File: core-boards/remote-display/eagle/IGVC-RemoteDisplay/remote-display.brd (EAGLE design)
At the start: 54.5 x 43 mm, 20 parts, among them IC1 ATMEGA2560-15AU, J1 ULCD-144G2, SW1 SPST_TACT-EVQQ2, U1 CC1101-MODULE, X1 16MHz, X2 MSTBA2

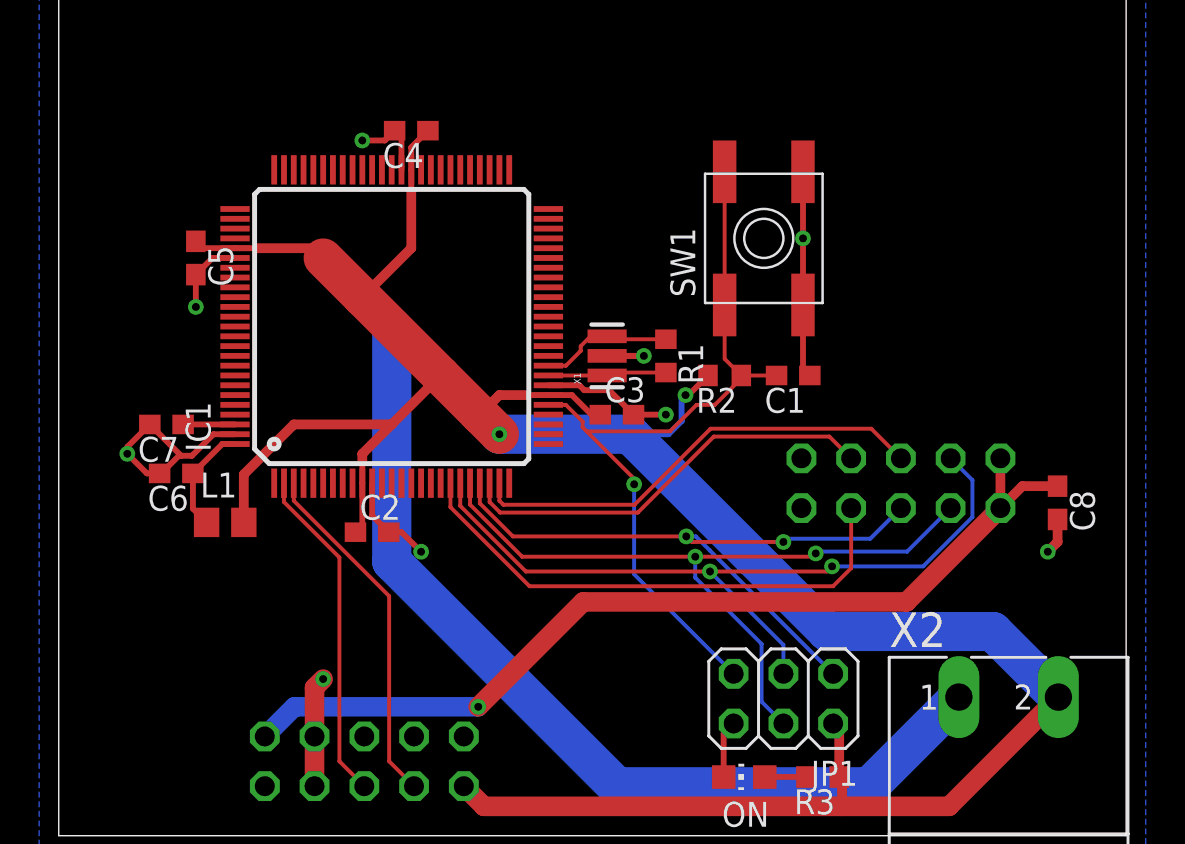
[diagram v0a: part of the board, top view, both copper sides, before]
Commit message: Replaced the MEGA2560 with a MEGA328p
This is just an option; if there are reasons for using the 2560, this can certainly be reverted
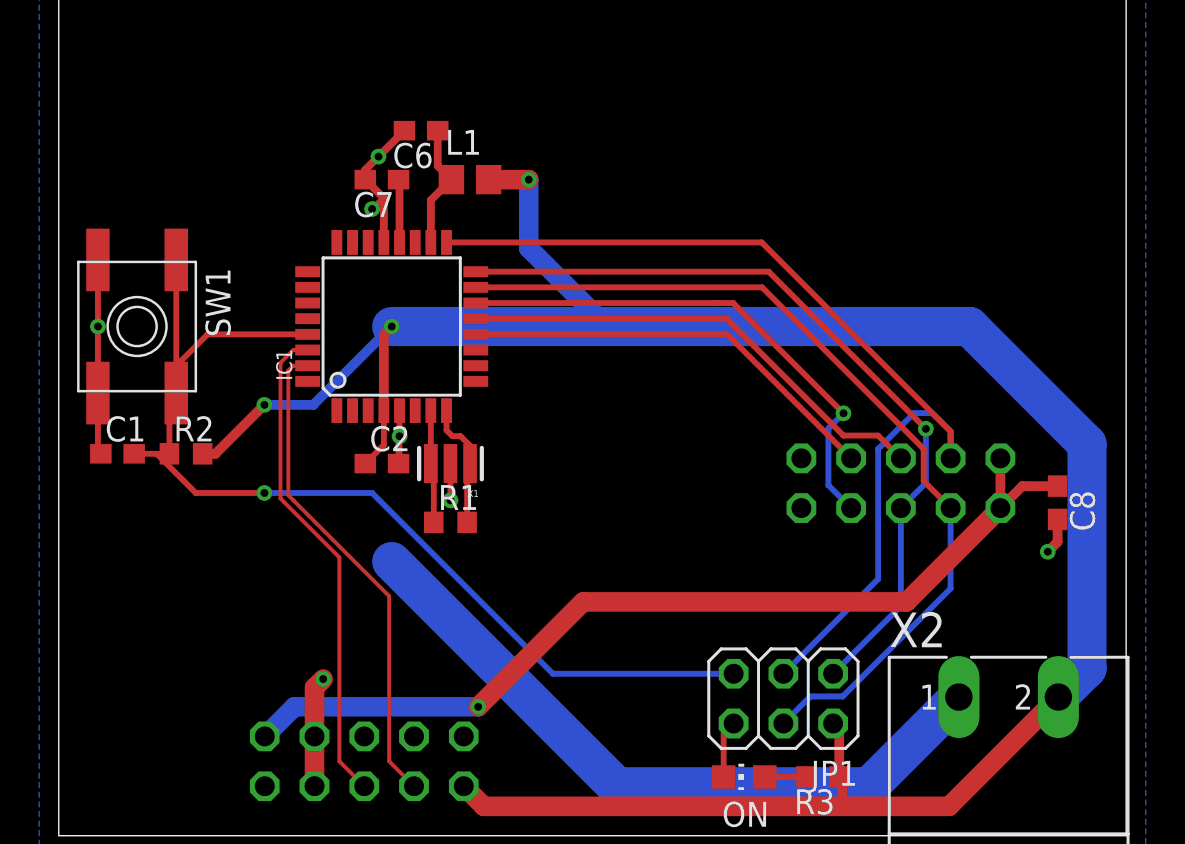
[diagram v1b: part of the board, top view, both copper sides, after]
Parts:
- removed C3, C4, C5: 100nF, resistor:C0603
- IC1: value ATMEGA2560-15AU -> ATMEGA8; device IGVC-Remote:TQFP100 -> atmel:TQFP32-08
- moved C1 34.7 mm to (3.00, 19.5), turned to 0 degrees
- moved SW1 32.3 mm to (4.00, 26.0), turned to 270 degrees
- moved R2 27.8 mm to (6.50, 19.5), turned to 0 degrees
- moved C6 21.5 mm to (18.5, 36.0)
- moved L1 21.5 mm to (21.0, 33.5)
- moved C7 16.7 mm to (16.5, 33.5)
- moved R1 13.9 mm to (20.0, 16.0), turned to 0 degrees
- moved X1 9.71 mm to (20.0, 19.0), turned to 180 degrees
- moved C2 3.54 mm to (16.5, 19.0)
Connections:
- net +5V: now also IC1.4; no longer C3.1, C4.1, C5.1, IC1.10, IC1.31, IC1.61, IC1.80
- net AREF: now also IC1.20; no longer IC1.98
- net AVCC: now also IC1.18; no longer IC1.100
- net CS: now also IC1.14; no longer IC1.19
- net GDO0: now also IC1.12; no longer IC1.23
- net GDO2: now also IC1.13; no longer IC1.24
- net GND: now also IC1.21, IC1.5; no longer C3.2, C4.2, C5.2, IC1.11, IC1.32, IC1.62, IC1.81, IC1.99
- net MISO: now also IC1.16; no longer IC1.22
- net MOSI: now also IC1.15; no longer IC1.21
- net RESET: now also IC1.29; no longer IC1.30
- net RX: now also IC1.30; no longer IC1.2
- net SCK: now also IC1.17; no longer IC1.20
- net TX: now also IC1.31; no longer IC1.3
- net XTAL1: now also IC1.7; no longer IC1.34
- net XTAL2: now also IC1.8; no longer IC1.33
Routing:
- net GND: track 102.5 -> 69.8 mm, vias 9 -> 7
- net +5V: track 134.8 -> 120.1 mm, vias 2 -> 3
- net RESET: track 39.9 -> 53.3 mm
- net SCK: track 40.1 -> 50.8 mm, vias 2 -> 0
- net RX: track 17.2 -> 25.0 mm
- net MOSI: track 38.1 -> 45.4 mm, vias 2 -> 0
- net TX: track 18.0 -> 25.0 mm
- net MISO: track 34.5 -> 40.8 mm, vias 2 -> 1
- net XTAL1: track 6.82 -> 5.77 mm
- net GDO2: track 23.7 -> 24.7 mm
- net AVCC: track 5.56 -> 6.43 mm
- net AREF: track 2.65 -> 3.23 mm
- net CS: track 26.8 -> 26.7 mm, vias 0 -> 1

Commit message: 20191117 Reworked schematic
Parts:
- removed J1: ULCD-144G2, IGVC-Remote:ULCD-144G2
- removed X2: MSTBA2, con-phoenix-508:MSTBA2
- added C10, C11: 10uF, rcl:C0603
- added C3: 0.1uF, resistor:C0603
- added C4: 100uF, rcl:PANASONIC_D
- added C5, C9: 1uF, rcl:C0603
- added J4: B2PS-VH(LF)(SN), RoboJackets-Connectors:B2PS-CENTERED
- added R4: 47R, resistor:R0805
- added T1: R-78E5.0-1.0, MotorBoardDev:R-78E
- added U2: ST7920, IGVC-Remote:ST7920-LCD
- added X3: (no value), IGVC-Connector:NRF24L01+PA+LNA
- C1: value 22p -> 22pF
- C2, C6, C7: value 100nF -> 0.1uF
- C8: value 100n -> 0.1uF
- U1: value CC1101-MODULE -> MIC550X; device IGVC-Remote:2X05 -> IGVC-Regulator:SOT23-DBV
- moved U1 140.8 mm to (1.50, -116.5), flipped to the top
- moved C8 68.1 mm to (113.5, 44.0)
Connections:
- removed net CS: IC1.14, U1.7
- removed net LCD_RST: J1.9
- new net LCD_CS: U2.4
- new net N$3: R4.1, U2.19
- new net RF_CS: IC1.14, X3.CSN
- new net VCC: C10.1, C4.+, J4.2, T1.1
- net +3V3: now also C5.1, U1.5, X3.VCC; no longer J1.10, U1.1, U1.2
- net +5V: now also C11.1, C3.1, C9.1, R4.2, T1.3, U1.1, U2.17, U2.2; no longer J1.1, X2.2
- net GDO0: now also X3.CE; no longer U1.8
- net GDO2: now also X3.IRQ; no longer U1.6
- net GND: now also C10.2, C11.2, C3.2, C4.-, C5.2, C9.2, J4.1, T1.2, U1.2, U2.1, U2.15, U2.20, X3.GND; no longer J1.7, J1.8, U1.10, U1.9, X2.1
- net MISO: now also X3.MISO; no longer U1.5
- net MOSI: now also U2.5, X3.MOSI; no longer U1.3
- net RX: no longer J1.5
- net SCK: now also U2.6, X3.SCK; no longer U1.4
- net TX: no longer J1.3
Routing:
- net +5V: track 120.1 -> 0.00 mm, vias 3 -> 0
- net GND: track 69.8 -> 0.00 mm, vias 7 -> 0
- net RESET: track 53.3 -> 0.00 mm, vias 1 -> 0
- net SCK: track 50.8 -> 0.00 mm
- net +3V3: track 48.3 -> 0.00 mm, vias 1 -> 0
- net MOSI: track 45.4 -> 0.00 mm
- net MISO: track 40.8 -> 0.00 mm, vias 1 -> 0
- net CS: track 26.7 -> 0.00 mm, vias 1 -> 0
- net RX: track 25.0 -> 0.00 mm
- net TX: track 25.0 -> 0.00 mm
- net GDO2: track 24.7 -> 0.00 mm
- net GDO0: track 21.8 -> 0.00 mm
- net XTAL2: track 6.51 -> 0.00 mm
- net AVCC: track 6.43 -> 0.00 mm
- net XTAL1: track 5.77 -> 0.00 mm
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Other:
- board size 54.5 x 43 mm -> 117.5 x 70 mm

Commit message: Finished routing, design review pending
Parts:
- removed J4: B2PS-VH(LF)(SN), RoboJackets-Connectors:B2PS-CENTERED
- removed X3: (no value), IGVC-Connector:NRF24L01+PA+LNA
- added D1, D2: RED, led:CHIP-LED0805
- added J1: B2PS-VH(LF)(SN), RoboJackets-Connectors:B2PS-CENTERED
- added R5, R6: 470R, resistor:R0603
- added R7: 10K, resistor:R0603
- added U$1: ROBOBUZZ1.0X, RoboJackets-Aesthetics:ROBOBUZZ_1.0X
- added X2: (no value), IGVC-Connector:NRF24L01+PA+LNA
- C1: value 22pF -> 0.1uF
- C10: value 10uF -> 1uF
- C11: value 10uF -> 22pF; device rcl:C0603 -> resistor:C0603
- C4: value 100uF -> 0.1uF; device rcl:PANASONIC_D -> resistor:C0603
- C5: value 1uF -> 0.1uF; device rcl:C0603 -> resistor:C0603
- C6: value 0.1uF -> 100uF; device resistor:C0603 -> rcl:PANASONIC_D
- C7: value 0.1uF -> 10uF; device resistor:C0603 -> rcl:C0603
- C8: value 0.1uF -> 1uF; device resistor:C0603 -> rcl:C0603
- C9: value 1uF -> 10uF
- R1: value 1M -> 10K; device resistor:R0603 -> adafruit:TRIM-3386
- R2: value 10K -> 47R; device resistor:R0603 -> resistor:R0805
- R3: value 470R -> 1M
- R4: value 47R -> 470R; device resistor:R0805 -> resistor:R0603
- U1: value MIC550X -> ST7920; device IGVC-Regulator:SOT23-DBV -> IGVC-Remote:ST7920-LCD
- U2: value ST7920 -> MIC550X; device IGVC-Remote:ST7920-LCD -> IGVC-Regulator:SOT23-DBV
- moved C11 182.0 mm to (54.0, 28.0), turned to 90 degrees
- moved C10 178.6 mm to (20.0, 35.0), turned to 90 degrees
- moved C4 170.4 mm to (34.5, 15.5)
- moved T1 165.1 mm to (24.5, 26.5), turned to 90 degrees
- moved C9 157.5 mm to (28.5, 28.5), turned to 270 degrees
- moved U1 147.5 mm to (92.0, 0.00), flipped to the bottom
- moved C3 142.1 mm to (36.5, 32.5), turned to 180 degrees
- moved C5 133.3 mm to (15.5, 9.50), turned to 270 degrees
- moved R4 87.1 mm to (15.0, 4.00), turned to 270 degrees
- moved C8 87.0 mm to (27.0, 35.0), turned to 90 degrees
- moved C1 72.8 mm to (74.0, 3.50), turned to 270 degrees
- moved R1 46.0 mm to (66.0, 14.5)
- moved SW1 43.5 mm to (47.5, 28.0), turned to 0 degrees
- moved U2 35.6 mm to (23.5, 35.0), turned to 90 degrees
- moved R3 33.0 mm to (33.0, 35.5)
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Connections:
- removed net RESET: C1.2, IC1.29, JP1.5, R2.1, SW1.B, SW1.B'
- removed net RX: IC1.30
- removed net TX: IC1.31
- removed net VCC: C10.1, C4.+, J4.2, T1.1
- new net !RESET: C11.2, IC1.29, JP1.5, R7.1, SW1.B, SW1.B'
- new net CONTRAST: R1.2, U1.3
- new net STAT1: IC1.24, R5.1
- new net STAT1_LED: D1.A, R5.2
- new net STAT2: IC1.25, R6.1
- new net STAT2_LED: D2.A, R6.2
- new net VIN: C6.+, C7.1, J1.2, T1.1
- net +3V3: now also C10.1, U2.5, X2.VCC; no longer C8.1, U1.5, X3.VCC
- net +5V: now also C1.1, C8.1, R1.3, R4.1, R7.2, U1.17, U1.2, U2.1, U2.3; no longer C11.1, C2.1, R3.1, R4.2, U1.1, U2.17, U2.2
- net AREF: now also C2.1; no longer C7.1
- net AVCC: now also C4.1; no longer C6.1
- net GDO0: now also X2.CE; no longer X3.CE
- net GDO2: now also X2.IRQ; no longer X3.IRQ
- net GND: now also C1.2, C11.1, C4.2, C6.-, D1.C, D2.C, J1.1, R1.1, U1.1, U1.15, U1.20, U2.2, X2.GND; no longer C1.1, C11.2, C4.-, C6.2, J4.1, U1.2, U2.1, U2.15, U2.20, X3.GND
- net LCD_CS: now also IC1.28, U1.4; no longer U2.4
- net MISO: now also X2.MISO; no longer X3.MISO
- net MOSI: now also U1.5, X2.MOSI; no longer U2.5, X3.MOSI
- net N$3: now also R2.1, U1.19; no longer R4.1, U2.19
- net PWR_LED: now also R4.2; no longer R3.2
- net RF_CS: now also X2.CSN; no longer X3.CSN
- net SCK: now also U1.6, X2.SCK; no longer U2.6, X3.SCK
- net XTAL1: now also R3.1; no longer R1.1
- net XTAL2: now also R3.2; no longer R1.2
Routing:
- net +5V: track 0.00 -> 150.9 mm, vias 0 -> 3
- net GND: track 0.00 -> 124.7 mm, vias 0 -> 8
- net MOSI: track 0.00 -> 95.8 mm, vias 0 -> 2
- net SCK: track 0.00 -> 92.8 mm, vias 0 -> 3
- net MISO: track 0.00 -> 59.6 mm, vias 0 -> 1
- net VIN: track 0.00 -> 42.9 mm
- net GDO0: track 0.00 -> 40.7 mm, vias 0 -> 1
- net GDO2: track 0.00 -> 39.2 mm
- net STAT2: track 0.00 -> 38.1 mm, vias 0 -> 2
- net STAT1: track 0.00 -> 37.9 mm, vias 0 -> 2
- net RF_CS: track 0.00 -> 34.0 mm, vias 0 -> 1
- net +3V3: track 0.00 -> 33.9 mm, vias 0 -> 2
- net LCD_CS: track 0.00 -> 32.6 mm
- net !RESET: track 0.00 -> 30.1 mm
- net CONTRAST: track 0.00 -> 9.17 mm
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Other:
- board size 117.5 x 70 mm -> 92 x 52.5 mm
- board text added: "- 9V +"
- board text added: "01/2020"
- board text added: "CONTRAST"
- board text added: "IGVC Remote Display"
- board text added: "Inst. No."
- board text added: "V1.0"

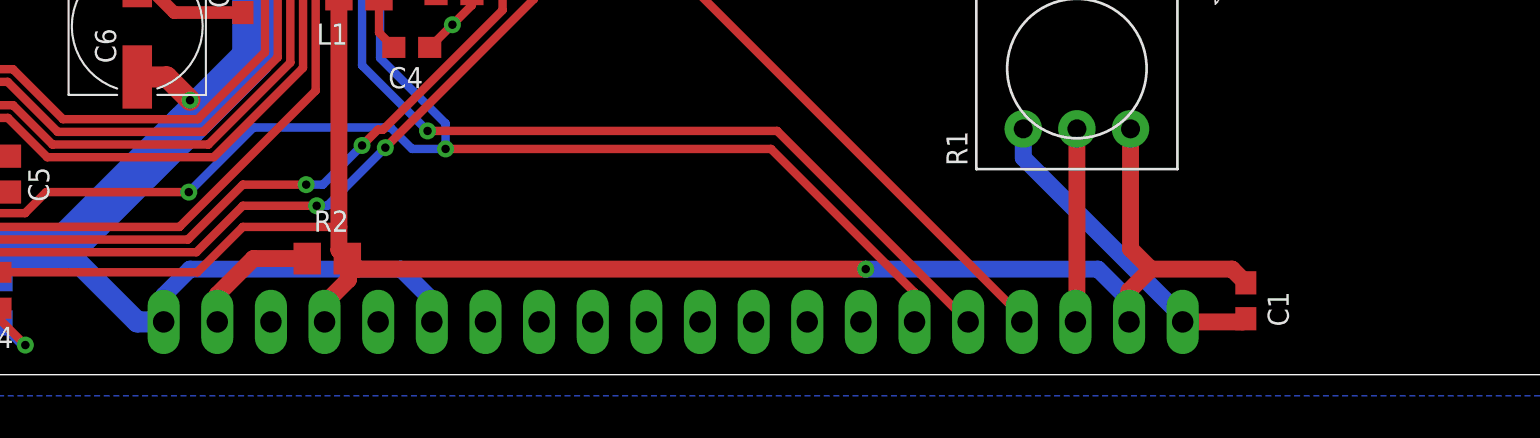
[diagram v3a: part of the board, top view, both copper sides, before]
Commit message: Redid component for LCD screen
And broke entire board
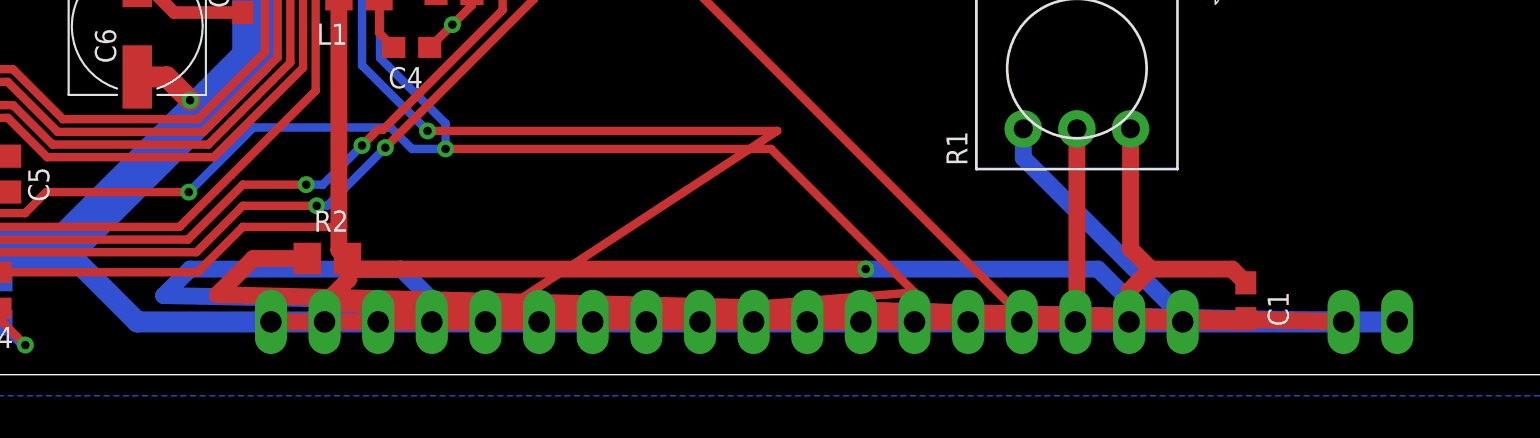
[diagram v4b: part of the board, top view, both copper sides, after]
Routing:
- net GND: track 124.7 -> 353.4 mm
- net N$3: track 6.26 -> 58.3 mm
- net +5V: track 150.9 -> 188.2 mm
- net CONTRAST: track 9.17 -> 42.2 mm
- net LCD_CS: track 32.6 -> 60.3 mm
- net SCK: track 92.8 -> 109.2 mm
- net MOSI: track 95.8 -> 99.6 mm
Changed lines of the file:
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@@
 <wire x1="12.5" y1="4.55" x2="12.5" y2="6" width="0.5" layer="16"/>
 <wire x1="15" y1="4.55" x2="15" y2="6" width="0.5" layer="16"/>
-<wire x1="22.75" y1="2.5" x2="21.5" y2="2.5" width="1" layer="16"/>
+<wire x1="81.17" y1="2.5" x2="21.5" y2="2.5" width="1" layer="16"/>
 <wire x1="21.5" y1="2.5" x2="18" y2="6" width="1" layer="16"/>
-<wire x1="35.45" y1="2.5" x2="35.45" y2="3.55" width="0.8" layer="16"/>
-<wire x1="22.75" y1="3.75" x2="22.75" y2="2.5" width="0.8" layer="16"/>
+<wire x1="63.39" y1="2.5" x2="35.45" y2="3.55" width="0.8" layer="16"/>
+<wire x1="22.75" y1="3.75" x2="81.17" y2="2.5" width="0.8" layer="16"/>
 <wire x1="35.45" y1="3.55" x2="34" y2="5" width="0.8" layer="16"/>
 <wire x1="34" y1="5" x2="24" y2="5" width="0.8" layer="16"/>
 <wire x1="24" y1="5" x2="22.75" y2="3.75" width="0.8" layer="16"/>
-<wire x1="71.01" y1="2.5" x2="73.85" y2="2.5" width="0.8" layer="1"/>
+<wire x1="27.83" y1="2.5" x2="73.85" y2="2.5" width="0.8" layer="1"/>
 <wire x1="73.85" y1="2.5" x2="74" y2="2.65" width="0.8" layer="1"/>
 <wire x1="63.46" y1="11.6425" x2="63.46" y2="10.268875" width="0.8" layer="16"/>
-<wire x1="71.01" y1="2.718875" x2="71.01" y2="2.5" width="0.8" layer="16"/>
+<wire x1="71.01" y1="2.718875" x2="27.83" y2="2.5" width="0.8" layer="16"/>
 <wire x1="63.46" y1="10.268875" x2="71.01" y2="2.718875" width="0.8" layer="16"/>
 <wire x1="37.35" y1="18" x2="37.35" y2="18.65" width="0.4" layer="1"/>
@@
 <wire x1="15.5" y1="8.65" x2="12.46" y2="8.65" width="0.8" layer="1"/>
 <wire x1="12.46" y1="8.65" x2="12.22" y2="8.41" width="0.8" layer="1"/>
-<wire x1="33" y1="32.5" x2="28.5" y2="27.65" width="0" layer="19" extent="1-1"/>
-<wire x1="35.65" y1="32.5" x2="33" y2="32.5" width="0" layer="19" extent="1-1"/>
+<wire x1="44.1" y1="26" x2="45.04" y2="34.73" width="0" layer="19" extent="1-1"/>
+<wire x1="36.4" y1="21.2074" x2="44.1" y2="26" width="0" layer="19" extent="1-1"/>
+<wire x1="35.6" y1="29.7926" x2="36.4" y2="21.2074" width="0" layer="19" extent="1-1"/>
+<wire x1="33" y1="32.5" x2="35.65" y2="32.5" width="0" layer="19" extent="1-1"/>
 <wire x1="27" y1="35.85" x2="33" y2="34.15" width="0" layer="19" extent="1-1"/>
 <wire x1="21" y1="37" x2="24.8" y2="35" width="0" layer="19" extent="1-1"/>
-<wire x1="36.4" y1="21.2074" x2="35.6" y2="29.7926" width="0" layer="19" extent="1-1"/>
-<wire x1="44.1" y1="26" x2="36.4" y2="21.2074" width="0" layer="19" extent="1-1"/>
-<wire x1="45.04" y1="34.73" x2="44.1" y2="26" width="0" layer="19" extent="1-1"/>
-<wire x1="63.46" y1="11.6425" x2="53.2" y2="25.6" width="0" layer="19" extent="1-1"/>
+<wire x1="28.5" y1="27.65" x2="33" y2="32.5" width="0" layer="19" extent="1-1"/>
+<wire x1="74" y1="2.65" x2="81.17" y2="2.5" width="0" layer="19" extent="1-1"/>
 </signal>
 <signal name="!RESET">
@@
 <wire x1="24.8" y1="34.05" x2="26.9" y2="34.05" width="0.5" layer="1"/>
 <wire x1="26.9" y1="34.05" x2="27" y2="34.15" width="0.5" layer="1"/>
-<wire x1="30.37" y1="2.5" x2="30.37" y2="3.37" width="0.8" layer="1"/>
+<wire x1="68.47" y1="2.5" x2="30.37" y2="3.37" width="0.8" layer="1"/>
 <wire x1="30.37" y1="3.37" x2="31.5" y2="4.5" width="0.8" layer="1"/>
 <wire x1="31.5" y1="4.5" x2="31.5" y2="5.45" width="0.8" layer="1"/>
@@
 <wire x1="26.5" y1="7" x2="31.05" y2="7" width="0.4" layer="1"/>
 <wire x1="24.35" y1="4.85" x2="26.5" y2="7" width="0.4" layer="1"/>
+<wire x1="31.45" y1="5.5" x2="30.37" y2="2.5" width="0" layer="19" extent="1-1"/>
 </signal>
 <signal name="AREF">
@@
 <via x="35.2484" y="11.5449875" extent="1-16" drill="0.4"/>
 <wire x1="35.2484" y1="11.5449875" x2="51.8050125" y2="11.5449875" width="0.4" layer="1"/>
-<wire x1="51.8050125" y1="11.5449875" x2="60.85" y2="2.5" width="0.4" layer="1"/>
+<wire x1="51.8050125" y1="11.5449875" x2="37.99" y2="2.5" width="0.4" layer="1"/>
 <wire x1="15.37439375" y1="12.162" x2="8.352" y2="12.162" width="0.4" layer="1"/>
 <wire x1="29.35" y1="14.5316125" x2="29.35" y2="19.90514375" width="0.4" layer="1"/>
@@
 <wire x1="33.2" y1="19.7" x2="33.2" y2="21.2074" width="0.4" layer="1"/>
 <wire x1="43.712" y1="36.058" x2="43.712" y2="30.212" width="0.4" layer="16"/>
-<wire x1="58.31" y1="3.8966125" x2="58.31" y2="2.5" width="0.4" layer="1"/>
+<wire x1="58.31" y1="3.8966125" x2="40.53" y2="2.5" width="0.4" layer="1"/>
 <wire x1="33" y1="15" x2="33" y2="19.5" width="0.4" layer="16"/>
 <wire x1="33" y1="15" x2="36.1016" y2="11.8984" width="0.4" layer="16"/>
@@
 <contactref element="R2" pad="1"/>
 <contactref element="U1" pad="19"/>
-<wire x1="25.29" y1="2.5" x2="25.29" y2="3.79" width="0.8" layer="1"/>
+<wire x1="78.63" y1="2.5" x2="25.29" y2="3.79" width="0.8" layer="1"/>
 <wire x1="27" y1="5.5" x2="29.55" y2="5.5" width="0.8" layer="1"/>
 <wire x1="25.29" y1="3.79" x2="27" y2="5.5" width="0.8" layer="1"/>
@@
 <wire x1="40.3632" y1="25.0294" x2="41.11399375" y2="25.0294" width="0.4" layer="1"/>
 <wire x1="41.11399375" y1="25.0294" x2="63.39" y2="2.75339375" width="0.4" layer="1"/>
-<wire x1="63.39" y1="2.75339375" x2="63.39" y2="2.5" width="0.4" layer="1"/>
+<wire x1="63.39" y1="2.75339375" x2="35.45" y2="2.5" width="0.4" layer="1"/>
 </signal>
 <signal name="VIN" class="1">
@@
 <contactref element="U1" pad="3"/>
 <wire x1="66" y1="11.6425" x2="66" y2="2.57" width="0.8" layer="1"/>
-<wire x1="66" y1="2.57" x2="65.93" y2="2.5" width="0.8" layer="1"/>
+<wire x1="66" y1="2.57" x2="32.91" y2="2.5" width="0.8" layer="1"/>
 </signal>
 <signal name="STAT1_LED">
